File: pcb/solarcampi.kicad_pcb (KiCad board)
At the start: 2 copper layers, 65 x 30 mm, 46 parts, among them J1 Vin 12V, J2 AVR-ISP-6, J3 FTDI_AVR, J4 Conn_02x20_Odd_Even, J5 FTDI_RPI, Q1 Q_NMOS_GDS, Q2 IRLML 2244, Q3 Q_NMOS_GDS, Q4 Q_NMOS_GDS, U1 INA226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

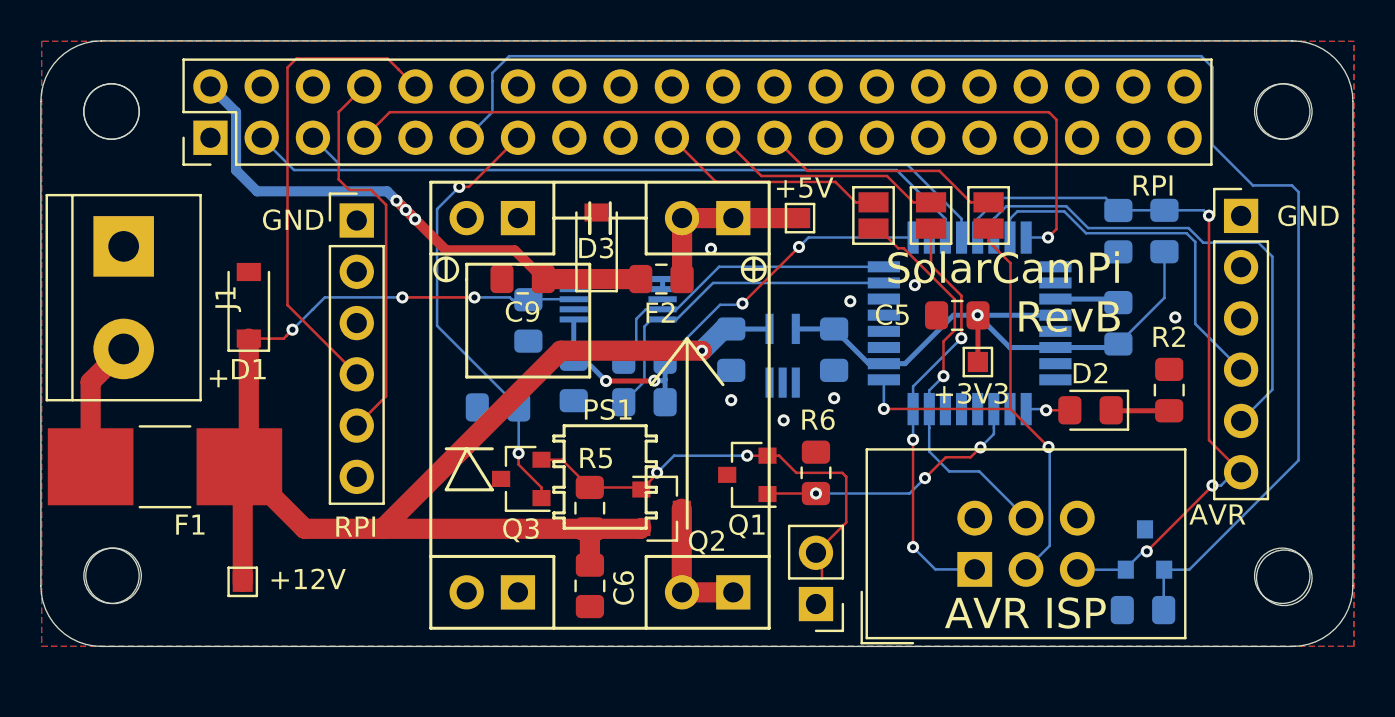
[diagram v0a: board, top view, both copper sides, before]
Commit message: Fix RevB errata
- Fix SOT23 NMOS pinout
- Fix AVR reset circuitry
- Add ceramic snubber to suppress ringing at input
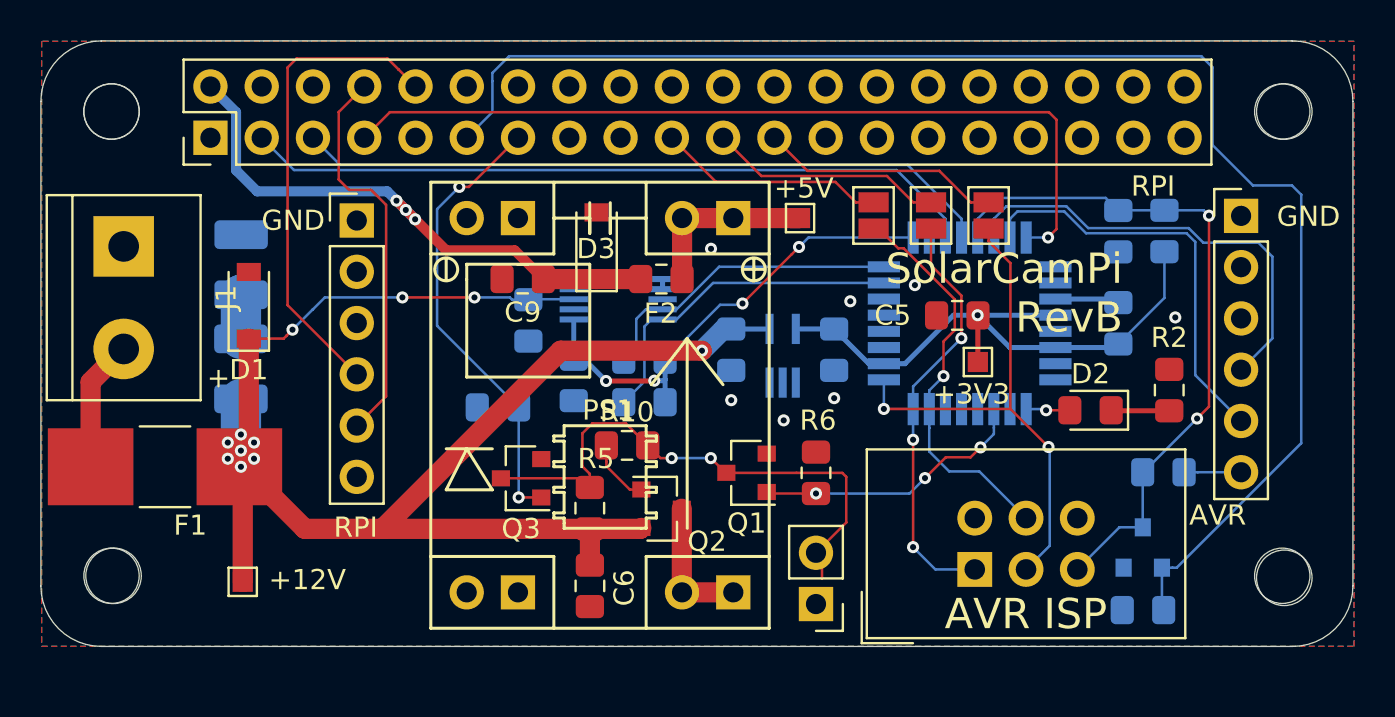
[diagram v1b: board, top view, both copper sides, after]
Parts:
- added C10: 100u, Capacitor_SMD:C_1210_3225Metric_Pad1.42x2.65mm_HandSolder, B.Cu at (59.9, 60.1)
- added C11: 100n, Capacitor_SMD:C_0805_2012Metric_Pad1.15x1.40mm_HandSolder, B.Cu at (105.6, 70.4)
- added R10: 1k, Resistor_SMD:R_0805_2012Metric_Pad1.15x1.40mm_HandSolder, F.Cu at (79.0, 69.0)
- added R9: 0.5R, Resistor_SMD:R_1210_3225Metric_Pad1.42x2.65mm_HandSolder, B.Cu at (59.9, 65.2)
- Q1, Q3, Q4: value Q_NMOS_GDS -> Q_NMOS_GSD
- moved Q4 0.15 mm to (104.6, 74.1)
- moved Q1 0.11 mm to (85.0, 70.4)
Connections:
- J3 pad 4: /TXD -> /RXD
- J3 pad 5: /RXD -> /TXD
- J3 pad 6: /~RST -> Net-(C11-Pad1)
- Q1 pad 2: Net-(JP2-Pad2) -> GND
- Q1 pad 3: GND -> Net-(JP2-Pad2)
- Q2 pad 1: Net-(JP2-Pad2) -> Net-(Q2-Pad1)
- Q3 pad 2: Net-(JP2-Pad2) -> GND
- Q3 pad 3: GND -> Net-(JP2-Pad2)
- Q4 pad 2: /~RST -> GND
- Q4 pad 3: GND -> /~RST
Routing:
- net Net-(JP2-Pad2): track 21.9 -> 26.8 mm
- net Net-(Q2-Pad1): track 0.00 -> 3.39 mm
- net +12V: track 75.6 -> 78.9 mm, vias 4 -> 11
- net Net-(C11-Pad1): track 0.00 -> 3.16 mm
- net /~RST: track 36.7 -> 34.1 mm, vias 3 -> 2
- net /RXD: track 24.8 -> 22.3 mm
- net /TXD: track 18.2 -> 20.7 mm
- net Net-(C10-Pad2): track 0.00 -> 2.19 mm
- net /PWR_OVR: track 21.9 -> 22.6 mm

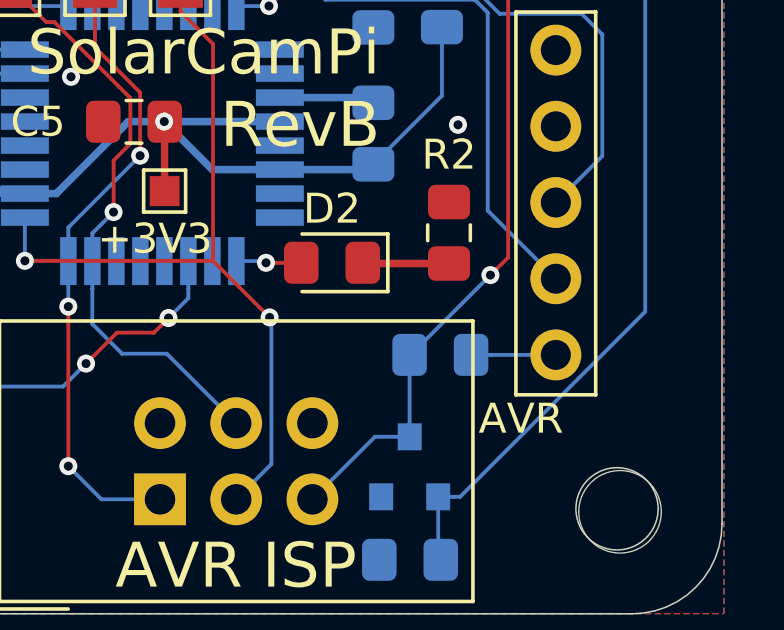
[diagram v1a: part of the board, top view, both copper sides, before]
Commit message: Optimize GND around C11
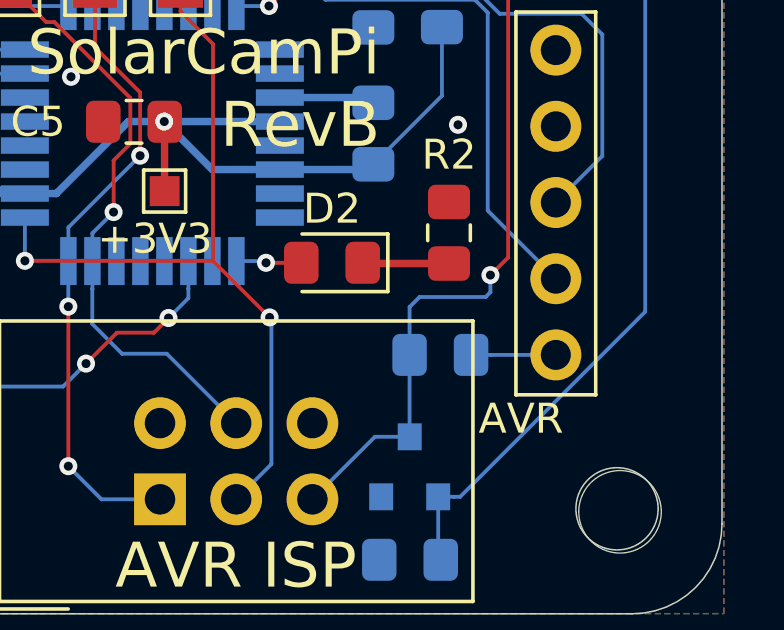
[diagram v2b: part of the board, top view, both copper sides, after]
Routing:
- net /~RST: track 34.1 -> 35.4 mm
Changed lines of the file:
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@@
     (thickness 1.6)
     (drawings 36)
-    (tracks 335)
+    (tracks 339)
     (zones 0)
     (modules 50)
@@
   (segment (start 107.87 67.12) (end 107.28 67.71) (width 0.127) (layer F.Cu) (net 5))
   (segment (start 104.62 70.37) (end 104.585 70.37) (width 0.127) (layer B.Cu) (net 5))
-  (segment (start 107.28 67.71) (end 104.62 70.37) (width 0.127) (layer B.Cu) (net 5))
+  (segment (start 104.585 68.775) (end 104.585 70.37) (width 0.127) (layer B.Cu) (net 5))
+  (segment (start 107.12 68.44) (end 104.92 68.44) (width 0.127) (layer B.Cu) (net 5))
+  (segment (start 107.28 67.71) (end 107.28 68.28) (width 0.127) (layer B.Cu) (net 5))
+  (segment (start 104.92 68.44) (end 104.585 68.775) (width 0.127) (layer B.Cu) (net 5))
+  (segment (start 107.28 68.28) (end 107.12 68.44) (width 0.127) (layer B.Cu) (net 5))
   (segment (start 52.465 65.899) (end 54.102 64.262) (width 1) (layer F.Cu) (net 6))
   (segment (start 52.465 70.1) (end 52.465 65.899) (width 1) (layer F.Cu) (net 6))

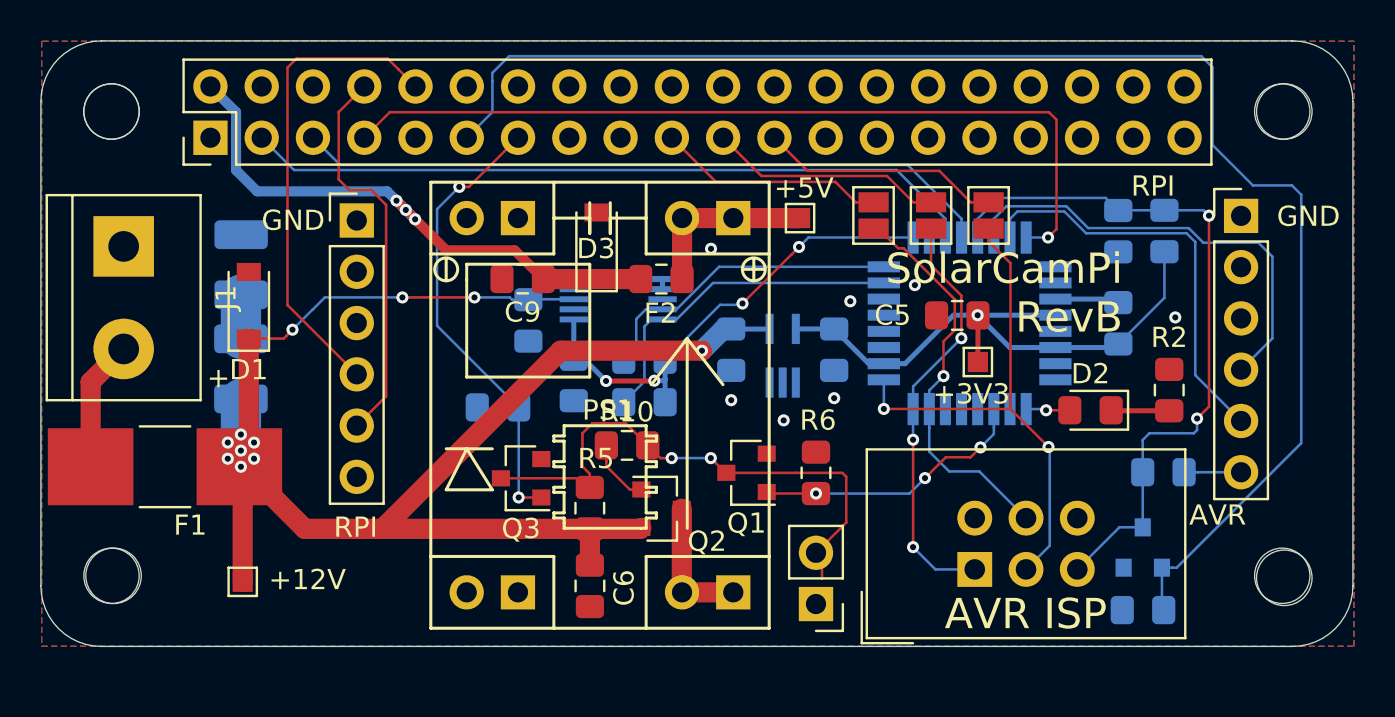
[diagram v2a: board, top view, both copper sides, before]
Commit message: Add current shunt
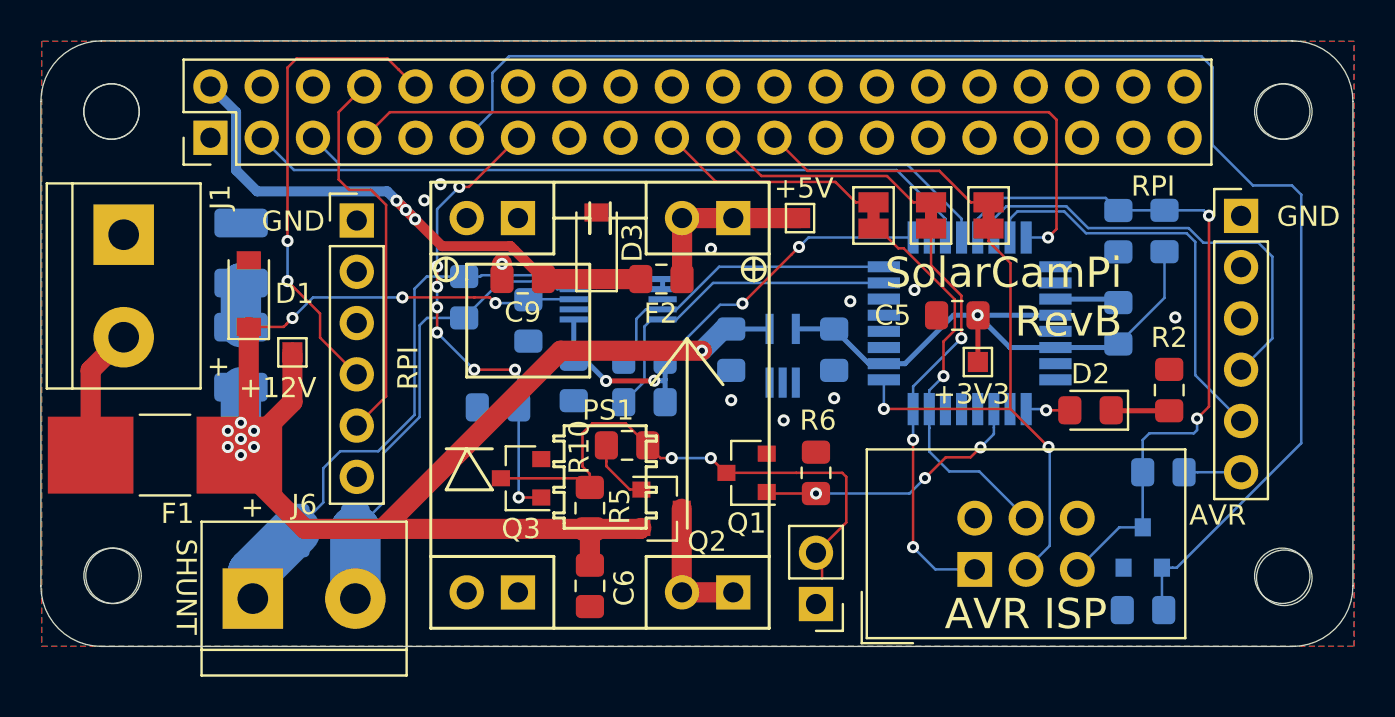
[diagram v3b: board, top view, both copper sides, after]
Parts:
- added C12: C, Capacitor_SMD:C_0805_2012Metric_Pad1.15x1.40mm_HandSolder, B.Cu at (71.0, 61.7)
- added J6: Shunt, solarcampi:TerminalBlock_bornier-2_P5.08mm, F.Cu at (60.5, 76.6)
- added R11: R, Resistor_SMD:R_1210_3225Metric_Pad1.42x2.65mm_HandSolder, B.Cu at (64.1, 73.3)
- JP3, JP4, JP5: footprint Jumper:SolderJumper-2_P1.3mm_Open_Pad1.0x1.5mm -> Jumper:SolderJumper-2_P1.3mm_Bridged_Pad1.0x1.5mm
- moved TP1 11.6 mm to (62.5, 64.4)
- moved C10 0.58 mm to (59.9, 59.5)
- moved J1 0.58 mm to (54.1, 58.6)
- moved D1 0.58 mm to (60.3, 61.5)
- moved F1 0.58 mm to (56.1, 69.5)
- moved R9 0.58 mm to (59.9, 64.7)
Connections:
- U1 pad 10: Net-(U1-Pad10) -> /SHUNT+
- U1 pad 9: Net-(U1-Pad9) -> /SHUNT-
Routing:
- net /SHUNT+: track 0.00 -> 28.0 mm
- net /SHUNT-: track 0.00 -> 23.6 mm
- net /PWR_OVR: track 22.6 -> 23.7 mm, vias 2 -> 8
- net GND: track 3.69 -> 4.44 mm, vias 7 -> 10
- net +12V: track 78.9 -> 79.5 mm
- net /TX: vias 0 -> 2
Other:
- board text added: "-"
- board text added: "SHUNT"
- board text added: "VDC"

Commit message: Update 3d models
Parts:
- PS1: value MP1584EN -> TPS63070-compat; footprint solarcampi:MP1584_buck_module -> tps63070-module:TPS63070-module-compat
- turned PS1 to 0 degrees
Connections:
- PS1 pad 3: GND -> /RPI_5V
- PS1 pad 4: /RPI_5V -> GND

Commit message: Update revision indictor to `RevC`
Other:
- board text added: "SolarCamPi RevC"
- board text removed: "SolarCamPi RevB"
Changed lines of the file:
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@@
     (effects (font (size 1.5 1.5) (thickness 0.3)) (justify right mirror))
   )
-  (gr_text "SolarCamPi\nRevB\n" (at 103.57 61.7) (layer F.SilkS)
+  (gr_text "SolarCamPi\nRevC\n" (at 103.57 61.7) (layer F.SilkS)
     (effects (font (size 1.5 1.5) (thickness 0.3)) (justify right))
   )
